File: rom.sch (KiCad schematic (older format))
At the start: 2 parts, among them U6 ROM

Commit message: Begin adding part numbers
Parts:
- C6: Cost (none) -> 0.078; MFG Name (none) -> KEMET; MFG Part Num (none) -> C412C334M5U5TA
- U6: Optional (none) -> ROM
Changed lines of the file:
@@
 F 2 "Package_DIP:DIP-42_W15.24mm_Socket_LongPads" H 5270 3585 50  0001 C CNN
 F 3 "DOCUMENTATION" H 5270 3585 50  0001 C CNN
+F 4 "ROM" H 5270 3585 50  0001 C CNN "Optional"
 	1    5270 3585
 	1    0    0    -1
@@
 F 2 "Package_DIP:DIP-42_W15.24mm_Socket_LongPads" H 8250 3585 50  0001 C CNN
 F 3 "DOCUMENTATION" H 8250 3585 50  0001 C CNN
+F 4 "ROM" H 8250 3585 50  0001 C CNN "Optional"
 	2    8250 3585
 	1    0    0    -1
@@
 F 2 "Raemixx500:C_Axial_L6.3mm_D2.5mm_P10.16mm" H 9093 3395 50  0001 C CNN
 F 3 "~" H 9055 3545 50  0001 C CNN
+F 4 "KEMET" H 9055 3545 50  0001 C CNN "MFG Name"
+F 5 "C412C334M5U5TA" H 9055 3545 50  0001 C CNN "MFG Part Num"
+F 6 "0.078" H 9055 3545 50  0001 C CNN "Cost"
 	1    9055 3545
 	1    0    0    -1

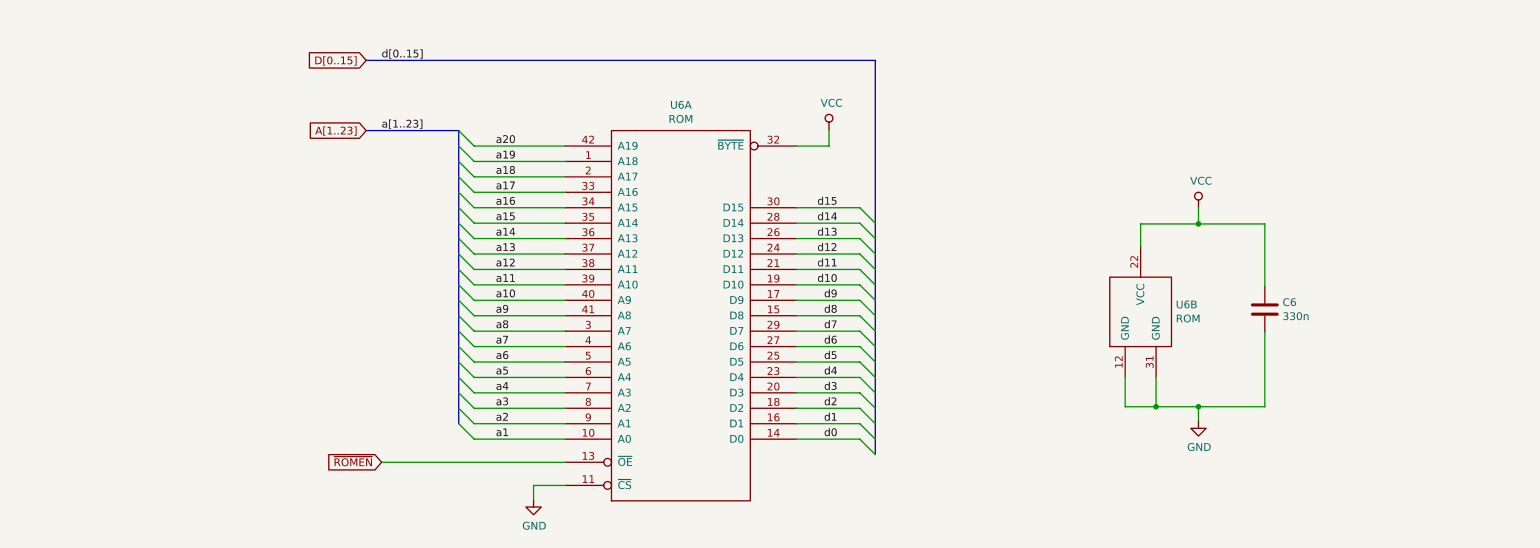
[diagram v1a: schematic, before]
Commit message: Add Kickstart switcher
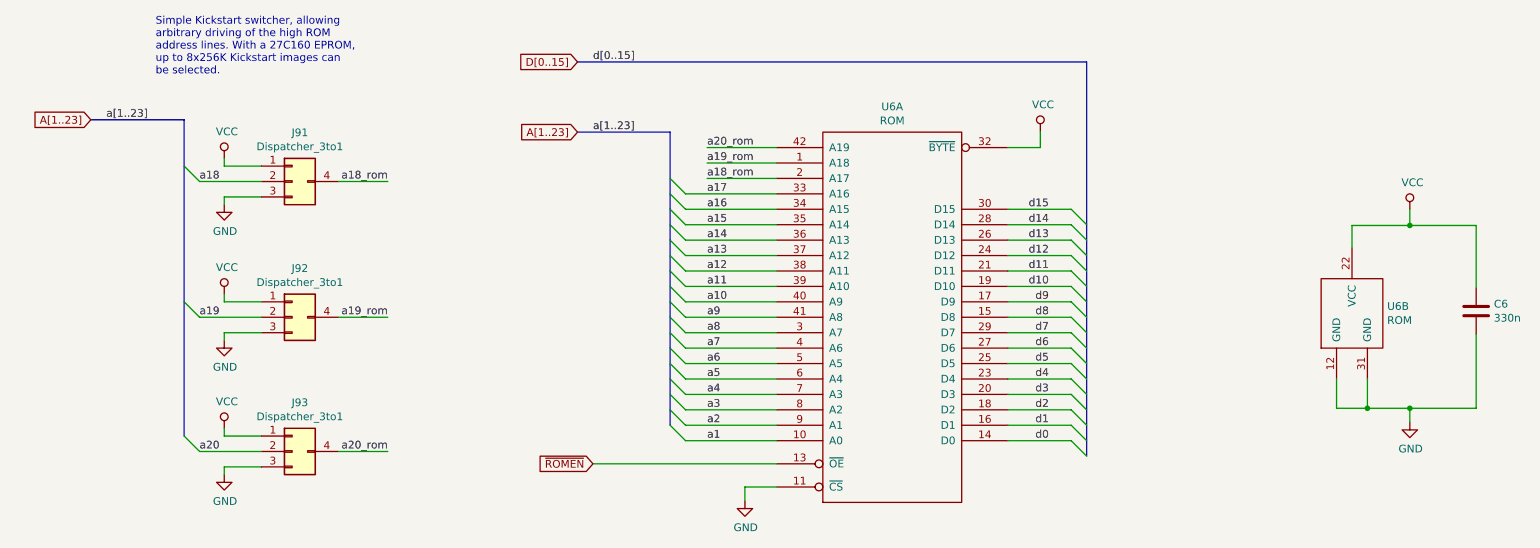
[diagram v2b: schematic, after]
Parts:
- added J91, J92, J93: Dispatcher_3to1, Raemixx500:Dispatcher_3to1, symbol Dispatcher:Dispatcher_3to1
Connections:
- net GND: now also J91.3 (In_3), J92.3 (In_3), J93.3 (In_3)
- net VCC: now also J91.1 (In_1), J92.1 (In_1), J93.1 (In_1)
- net a18: now also J91.2 (In_2); no longer U6.2 (A17)
- net a19: now also J92.2 (In_2); no longer U6.1 (A18)
- net a20: now also J93.2 (In_2); no longer U6.42 (A19)
- new net a18_rom: J91.4 (Out), U6.2 (A17)
- new net a19_rom: J92.4 (Out), U6.1 (A18)
- new net a20_rom: J93.4 (Out), U6.42 (A19)
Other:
- note added: "Simple Kickstart switcher, allowing\narbitrary driving of the high ROM\naddress lines. With a 27C160 EPROM,\nup to 8x256K Kickstart images can\nbe selected."
- moved on the sheet: C6, U6A, U6B

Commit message: (Try to) Identify the minimum set of required components
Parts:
- C6: Required (none) -> R
- U6: Required (none) -> Y
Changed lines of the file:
@@
 F 3 "DOCUMENTATION" H 6640 3595 50  0001 C CNN
 F 4 "ROM" H 6640 3595 50  0001 C CNN "Optional"
+F 5 "Y" H 6640 3595 50  0001 C CNN "Required"
 	1    6640 3595
 	1    0    0    -1
@@
 F 3 "DOCUMENTATION" H 9620 3595 50  0001 C CNN
 F 4 "ROM" H 9620 3595 50  0001 C CNN "Optional"
+F 5 "Y" H 9620 3595 50  0001 C CNN "Required"
 	2    9620 3595
 	1    0    0    -1
@@
 F 5 "C412C334M5U5TA" H 10425 3555 50  0001 C CNN "MFG Part Num"
 F 6 "0.078" H 10425 3555 50  0001 C CNN "Cost"
+F 7 "R" H 10425 3555 50  0001 C CNN "Required"
 	1    10425 3555
 	1    0    0    -1
@@
 Wire Wire Line
 	2150 4465 2550 4465
+Text Notes 1865 2030 0    50   ~ 0
+Simple Kickstart switcher, allowing\narbitrary driving of the high ROM\naddress lines. With a 27C160 EPROM,\nup to 8x256K Kickstart images can\nbe selected.
 Wire Bus Line
 	2050 2315 2050 4365
@@
 Wire Bus Line
 	5200 2395 5200 4295
-Text Notes 1865 2030 0    50   ~ 0
-Simple Kickstart switcher, allowing\narbitrary driving of the high ROM\naddress lines. With a 27C160 EPROM,\nup to 8x256K Kickstart images can\nbe selected.
 $EndSCHEMATC

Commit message: Rename "Optional" Field to "Section"
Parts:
- U6: Optional ROM -> (none); Section (none) -> ROM
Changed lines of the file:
@@
 F 2 "Package_DIP:DIP-42_W15.24mm_Socket_LongPads" H 6640 3595 50  0001 C CNN
 F 3 "DOCUMENTATION" H 6640 3595 50  0001 C CNN
-F 4 "ROM" H 6640 3595 50  0001 C CNN "Optional"
+F 4 "ROM" H 6640 3595 50  0001 C CNN "Section"
 F 5 "Y" H 6640 3595 50  0001 C CNN "Required"
 	1    6640 3595
@@
 F 2 "Package_DIP:DIP-42_W15.24mm_Socket_LongPads" H 9620 3595 50  0001 C CNN
 F 3 "DOCUMENTATION" H 9620 3595 50  0001 C CNN
-F 4 "ROM" H 9620 3595 50  0001 C CNN "Optional"
+F 4 "ROM" H 9620 3595 50  0001 C CNN "Section"
 F 5 "Y" H 9620 3595 50  0001 C CNN "Required"
 	2    9620 3595
